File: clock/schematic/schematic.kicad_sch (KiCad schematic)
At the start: 8 parts, among them U1 L78L05_TO92

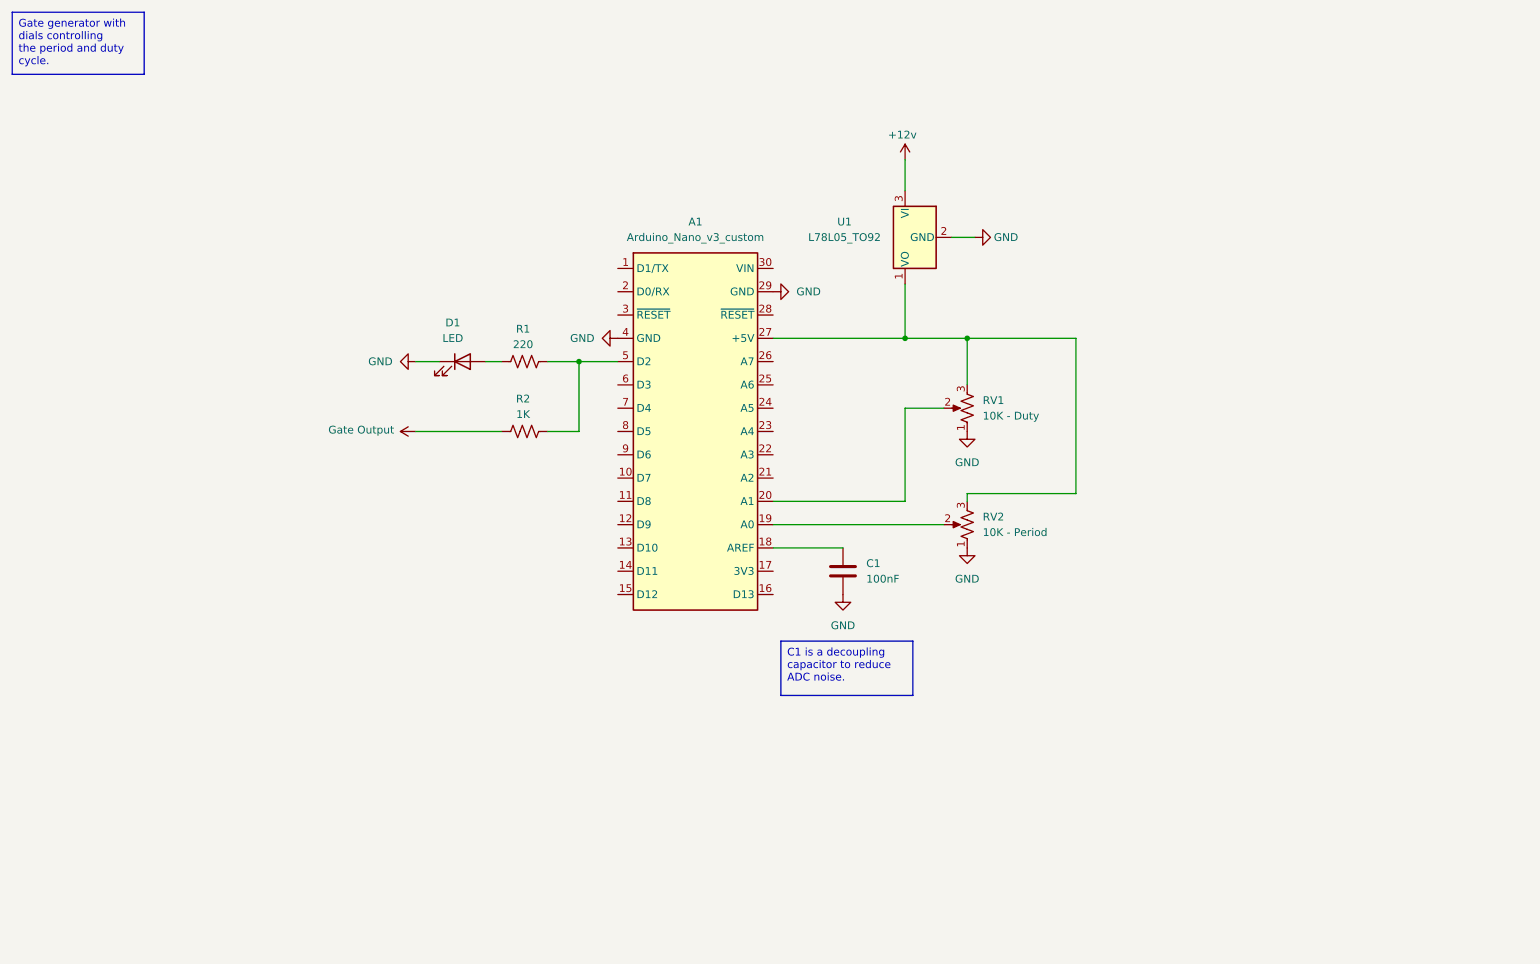
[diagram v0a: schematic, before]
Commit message: Update clock schematic
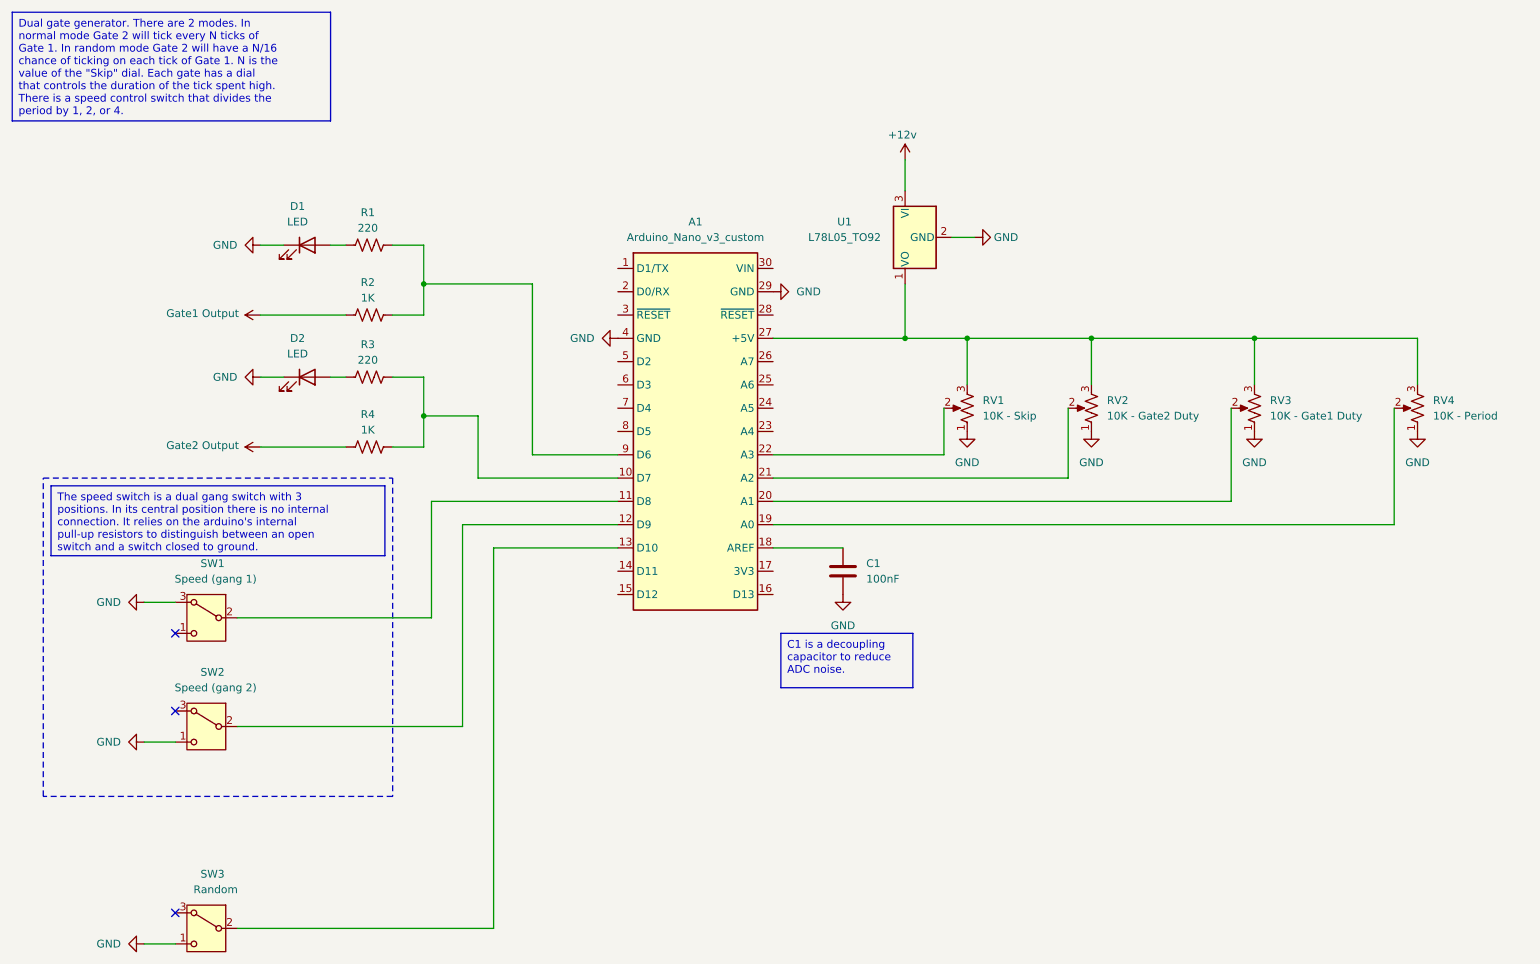
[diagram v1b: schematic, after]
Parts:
- added D2: LED, symbol Device:LED
- added R3: 220, symbol Device:R_US
- added R4: 1K, symbol Device:R_US
- added RV3: 10K - Gate1 Duty, symbol Device:R_Potentiometer_US
- added RV4: 10K - Period, symbol Device:R_Potentiometer_US
- added SW1: Speed (gang 1), Button_Switch_SMD:Nidec_Copal_CAS-120A, symbol Switch:SW_Nidec_CAS-120A1
- added SW2: Speed (gang 2), Button_Switch_SMD:Nidec_Copal_CAS-120A, symbol Switch:SW_Nidec_CAS-120A1
- added SW3: Random, Button_Switch_SMD:Nidec_Copal_CAS-120A, symbol Switch:SW_Nidec_CAS-120A1
- RV1: value 10K - Duty -> 10K - Skip
- RV2: value 10K - Period -> 10K - Gate2 Duty
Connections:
- net GND: now also D2.1 (K), RV3.1, RV4.1, SW1.3 (A), SW2.1 (C), SW3.1 (C)
- net at RV1.2: now also A1.22 (A3); no longer A1.20 (A1)
- net at A1.27 (+5V), RV1.3, RV2.3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: now also RV3.3, RV4.3
- net at R1.2, R2.2: now also A1.9 (D6); no longer A1.5 (D2)
- net at A1.10 (D7): now also R3.2, R4.2
- net at A1.11 (D8): now also SW1.2 (B)
- net at A1.12 (D9): now also SW2.2 (B)
- net at A1.13 (D10): now also SW3.2 (B)
- net at A1.19 (A0): now also RV4.2; no longer RV2.2
- net at A1.21 (A2): now also RV2.2
- net Gate Output renamed Gate1 Output
- new net: A1.20 (A1), RV3.2
- new net: D2.2 (A), R3.1
- new net Gate2 Output: R4.1
- no-connect marks 0 -> 3
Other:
- moved on the sheet: D1, R1, R2, RV2
